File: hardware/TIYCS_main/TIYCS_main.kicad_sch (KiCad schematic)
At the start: 50 parts, among them J1 USB4105-GF-A, J2 12vPWM, J3 WS2812B, J4 UART, J5 ExtSensor, J6 Terminal, J7 Barrel_Jack_Switch, J8 pinHeaders, Q1 NCE4060K, Q2 NCE4060K, Q3 2N7002, Q4 NCE4060K, Q5 NCE4060K, SW1 SW_Push, SW2 SW_Push, U1 ESP32-WROOM-32U, U2 CH340N, U3 MCP1703A-3302_SOT23

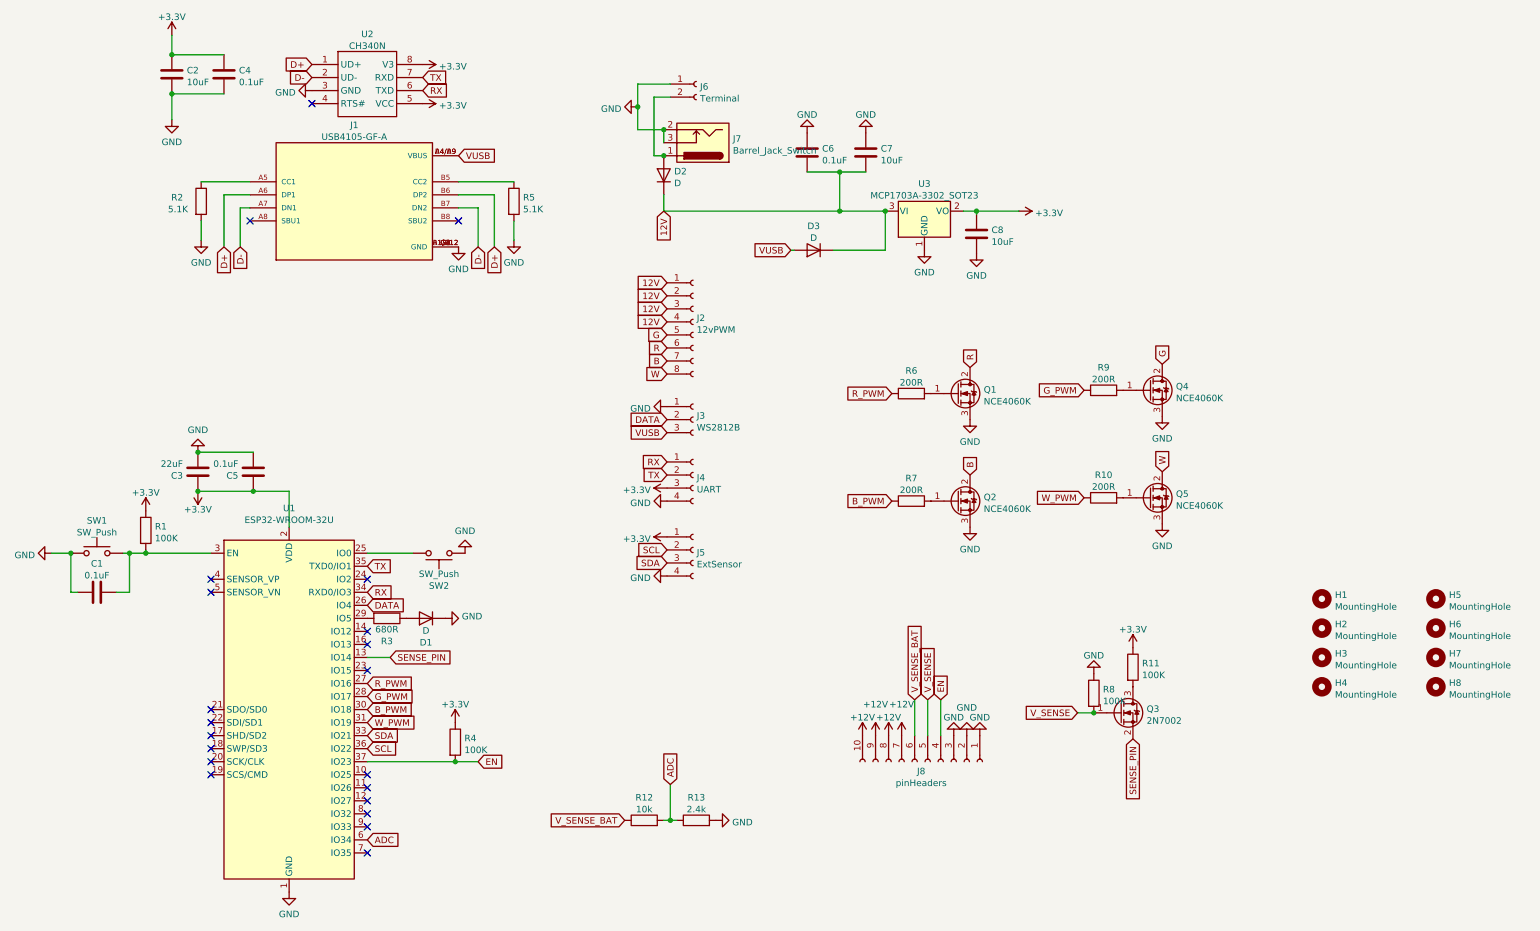
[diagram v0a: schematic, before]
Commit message: Start with new LDO, fuse
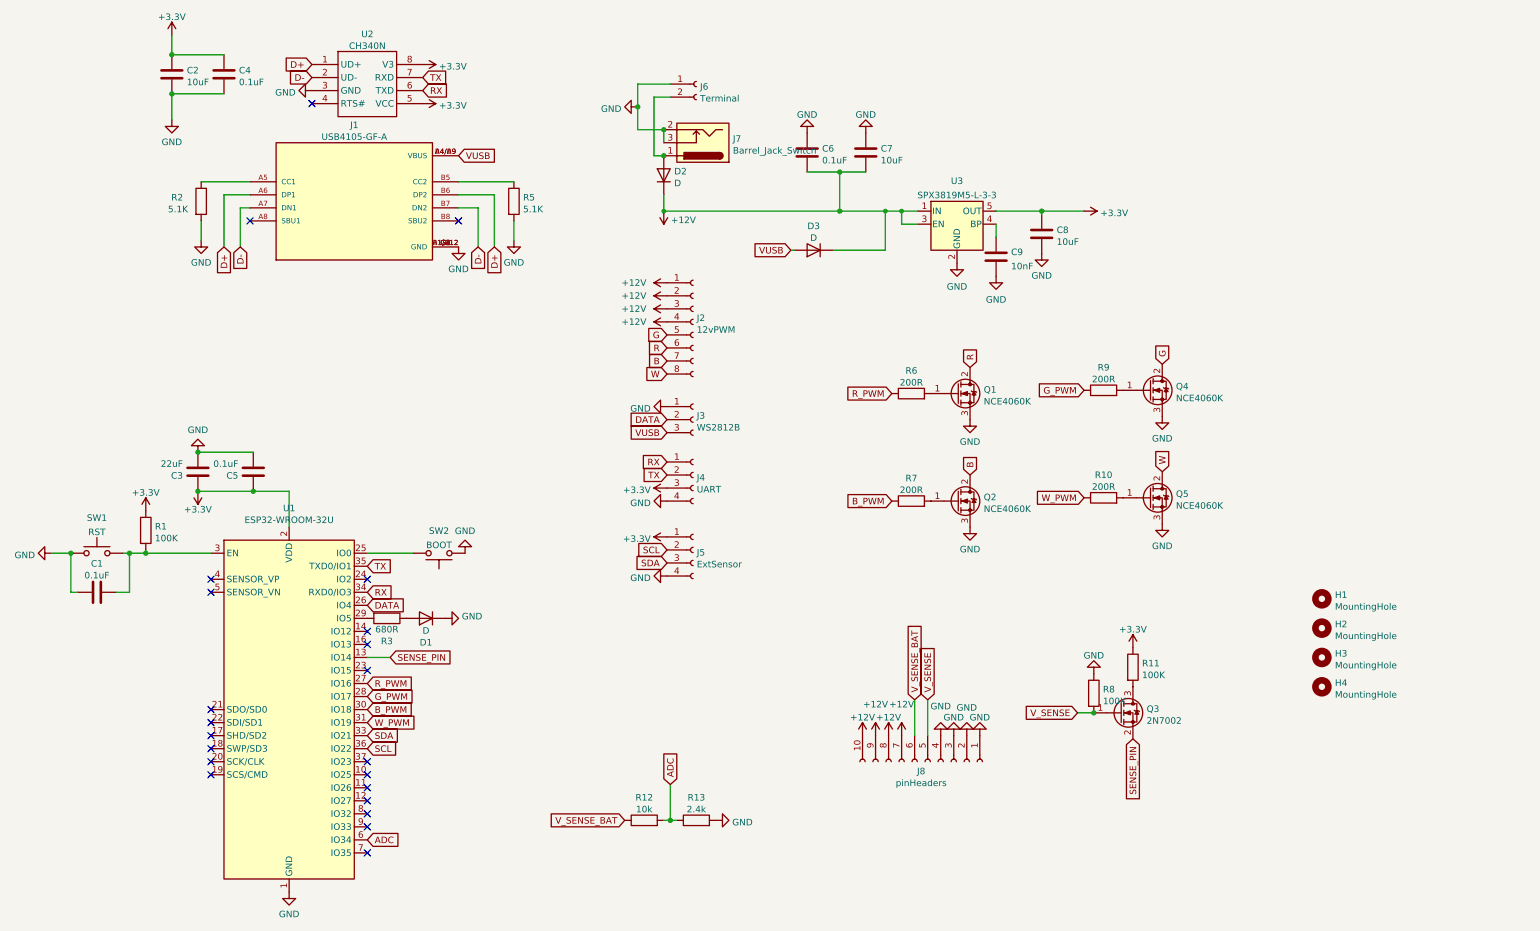
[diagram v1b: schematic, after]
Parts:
- removed H5, H6, H7, H8: MountingHole, MountingHole:MountingHole_3mm_Pad, symbol Mechanical:MountingHole
- removed R4: 100K, Resistor_SMD:R_0402_1005Metric, symbol Device:R
- removed U3: MCP1703A-3302_SOT23, Package_TO_SOT_SMD:SOT-23, symbol Regulator_Linear:MCP1703A-3302_SOT23
- added C9: 10nF, symbol Device:C
- added U3: SPX3819M5-L-3-3, Package_TO_SOT_SMD:SOT-23-5, symbol Regulator_Linear:SPX3819M5-L-3-3
- SW1: value SW_Push -> RST
- SW2: value SW_Push -> BOOT
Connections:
- net 12V is gone; now on net +12V: C6.2, C7.2, D2.1 (K), D3.1 (K), J2.1 (Pin_1), J2.2 (Pin_2), J2.3 (Pin_3), J2.4 (Pin_4)
- net +12V: now also U3.1 (IN), U3.3 (EN)
- net +3V3: now also U3.5 (OUT)
- net GND: now also J8.4 (Pin_4), C9.2, U3.2 (GND)
- net EN: no longer names the net of U1.37 (IO23)
- net EN: no longer J8.4 (Pin_4)
- new net: C9.1, U3.4 (BP)
- no-connect marks 21 -> 22
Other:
- moved on the sheet: C8

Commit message: First version of ledPanel: board outline + pins
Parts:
- C9: footprint (none) -> Capacitor_SMD:C_0402_1005Metric; JLCPCB (none) -> C15195
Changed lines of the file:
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@@
       (effects (font (size 1.27 1.27)) (justify left))
     )
-    (property "Footprint" "" (id 2) (at 208.6102 60.96 0)
+    (property "Footprint" "Capacitor_SMD:C_0402_1005Metric" (id 2) (at 208.6102 60.96 0)
       (effects (font (size 1.27 1.27)) hide)
     )
     (property "Datasheet" "~" (id 3) (at 207.645 57.15 0)
+      (effects (font (size 1.27 1.27)) hide)
+    )
+    (property "JLCPCB" " C15195 " (id 4) (at 207.645 57.15 0)
       (effects (font (size 1.27 1.27)) hide)
     )
@@
     )
     (path "/a6506404-fdc7-4490-bc6e-94643a9195be"
-      (reference "C9") (unit 1) (value "10nF") (footprint "")
+      (reference "C9") (unit 1) (value "10nF") (footprint "Capacitor_SMD:C_0402_1005Metric")
     )
     (path "/db090710-95ea-418e-b1d7-4e68f614b9ba"

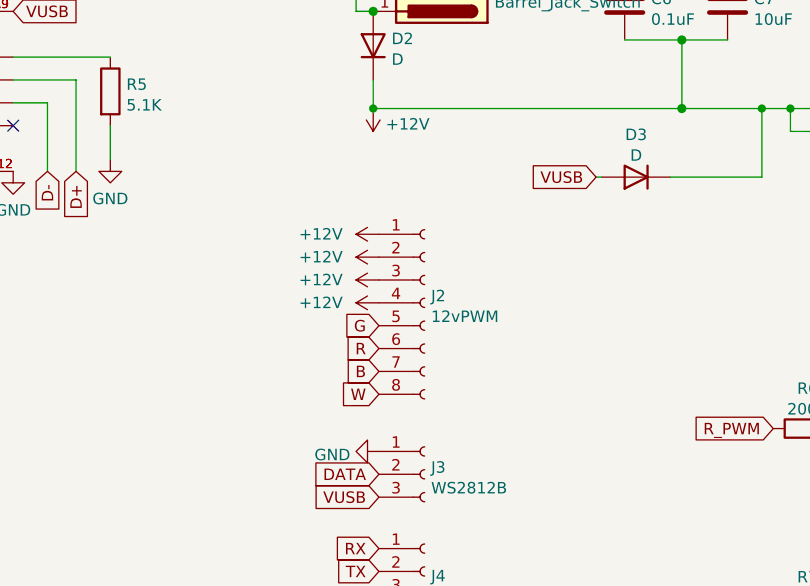
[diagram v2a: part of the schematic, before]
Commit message: Connector on motherboard aligned with ledPanel
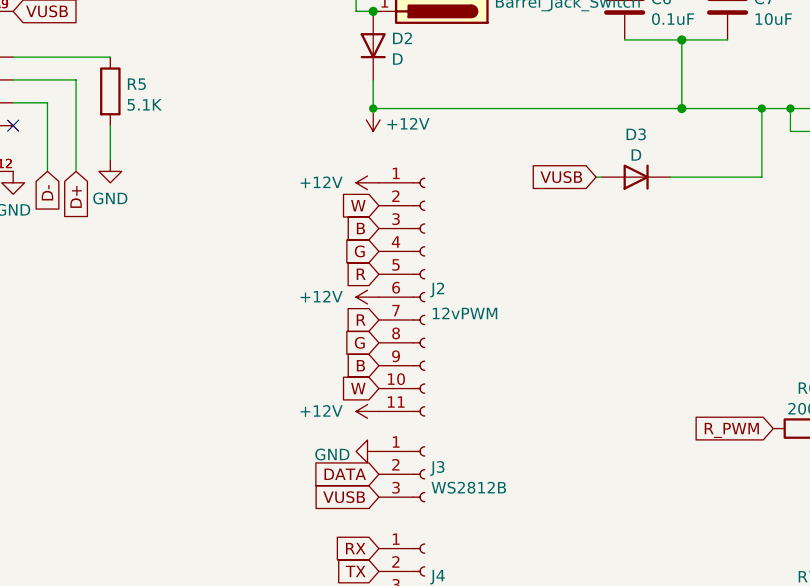
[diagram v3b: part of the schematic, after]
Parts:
- removed J2: 12vPWM, Connector_PinHeader_2.54mm:PinHeader_1x08_P2.54mm_Vertical, symbol Connector:Conn_01x08_Female
- added J2: 12vPWM, Connector_PinHeader_2.54mm:PinHeader_1x11_P2.54mm_Vertical, symbol Connector:Conn_01x11_Female
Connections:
- net +12V: now also J2.1 (Pin_1), J2.11 (Pin_11), J2.6 (Pin_6)
- net B: now also J2.3 (Pin_3), J2.9 (Pin_9)
- net G: now also J2.4 (Pin_4), J2.8 (Pin_8)
- net R: now also J2.5 (Pin_5), J2.7 (Pin_7)
- net W: now also J2.10 (Pin_10), J2.2 (Pin_2)

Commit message: Ordered hardware
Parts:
- added SW?: BTN, Switches:TACTILE_SWITCH_SMD_6.0X3.5MM, symbol Switch:SW_Push
- C2, C8: footprint Capacitor_SMD:C_0402_1005Metric -> Capacitor_SMD:C_0603_1608Metric
- C7: footprint Capacitor_SMD:C_0402_1005Metric -> Capacitor_SMD:C_0603_1608Metric; JLCPCB C15525 -> (none)
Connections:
- net GND: now also SW?.1
- net at U1.23 (IO15): now also SW?.2
- no-connect marks 22 -> 21
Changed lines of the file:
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@@
   (no_connect (at 85.09 120.015))
   (no_connect (at 85.09 132.715))
-  (no_connect (at 85.09 137.795))
   (no_connect (at 85.09 158.115))
   (no_connect (at 85.09 160.655))
@@
     (stroke (width 0) (type solid) (color 0 0 0 0))
   )
+  (wire (pts (xy 85.09 137.795) (xy 103.505 137.795))
+    (stroke (width 0) (type default) (color 0 0 0 0))
+  )
   (wire (pts (xy 207.645 50.8) (xy 207.645 53.34))
     (stroke (width 0) (type default) (color 0 0 0 0))
@@
       (effects (font (size 1.27 1.27)) (justify left))
     )
-    (property "Footprint" "Capacitor_SMD:C_0402_1005Metric" (id 2) (at 47.9552 25.4 0)
+    (property "Footprint" "Capacitor_SMD:C_0603_1608Metric" (id 2) (at 47.9552 25.4 0)
       (effects (font (size 1.27 1.27)) hide)
     )
@@
     )
     (property "Datasheet" "" (id 3) (at 202.565 109.855 0)
+      (effects (font (size 1.27 1.27)) hide)
+    )
+    (pin "1")
+  )
+  (symbol (lib_id "power:GND") (at 113.665 137.795 180) (unit 1)
+    (in_bom yes) (on_board yes) (fields_autoplaced)
+    (property "Reference" "#PWR?" (id 0) (at 113.665 131.445 0)
+      (effects (font (size 1.27 1.27)) hide)
+    )
+    (property "Value" "GND" (id 1) (at 113.665 133.4706 0))
+    (property "Footprint" "" (id 2) (at 113.665 137.795 0)
+      (effects (font (size 1.27 1.27)) hide)
+    )
+    (property "Datasheet" "" (id 3) (at 113.665 137.795 0)
       (effects (font (size 1.27 1.27)) hide)
     )
@@
     (pin "2")
   )
+  (symbol (lib_id "Switch:SW_Push") (at 108.585 137.795 180) (unit 1)
+    (in_bom yes) (on_board yes) (fields_autoplaced)
+    (property "Reference" "SW?" (id 0) (at 108.585 133.4475 0))
+    (property "Value" "BTN" (id 1) (at 108.585 136.2226 0))
+    (property "Footprint" "Switches:TACTILE_SWITCH_SMD_6.0X3.5MM" (id 2) (at 108.585 142.875 0)
+      (effects (font (size 1.27 1.27)) hide)
+    )
+    (property "Datasheet" "~" (id 3) (at 108.585 142.875 0)
+      (effects (font (size 1.27 1.27)) hide)
+    )
+    (pin "1")
+    (pin "2")
+  )
   (symbol (lib_id "Mechanical:MountingHole") (at 271.145 140.97 0) (unit 1)
     (in_bom yes) (on_board yes) (fields_autoplaced)
@@
       (effects (font (size 1.27 1.27)) (justify left))
     )
-    (property "Footprint" "Capacitor_SMD:C_0402_1005Metric" (id 2) (at 217.5002 56.515 0)
+    (property "Footprint" "Capacitor_SMD:C_0603_1608Metric" (id 2) (at 217.5002 56.515 0)
       (effects (font (size 1.27 1.27)) hide)
     )
@@
       (effects (font (size 1.27 1.27)) (justify left))
     )
-    (property "Footprint" "Capacitor_SMD:C_0402_1005Metric" (id 2) (at 183.2102 40.64 0)
+    (property "Footprint" "Capacitor_SMD:C_0603_1608Metric" (id 2) (at 183.2102 40.64 0)
       (effects (font (size 1.27 1.27)) hide)
     )
@@
       (effects (font (size 1.27 1.27)) hide)
     )
-    (property "JLCPCB" " C15525" (id 4) (at 182.245 36.83 0)
+    (property "JLCPCB" "" (id 4) (at 182.245 36.83 0)
       (effects (font (size 1.27 1.27)) hide)
     )
@@
       (reference "#PWR0147") (unit 1) (value "GND") (footprint "")
     )
+    (path "/a9cb1444-eba6-4ddf-88fb-081d86707002"
+      (reference "#PWR?") (unit 1) (value "GND") (footprint "")
+    )
     (path "/8c637d7d-c3ec-4153-9e1f-46e8fe712d7c"
       (reference "C1") (unit 1) (value "0.1uF") (footprint "Capacitor_SMD:C_0402_1005Metric")
     )
     (path "/6d23f2b3-8b15-4422-b7ea-fcbb1a61eb6b"
-      (reference "C2") (unit 1) (value "10uF") (footprint "Capacitor_SMD:C_0402_1005Metric")
+      (reference "C2") (unit 1) (value "10uF") (footprint "Capacitor_SMD:C_0603_1608Metric")
     )
     (path "/63c7647a-7f88-4811-aeb6-42a50ac287d8"
@@
     )
     (path "/e3e8dee4-7597-4ebc-89e5-4bbb58b34d69"
-      (reference "C7") (unit 1) (value "10uF") (footprint "Capacitor_SMD:C_0402_1005Metric")
+      (reference "C7") (unit 1) (value "10uF") (footprint "Capacitor_SMD:C_0603_1608Metric")
     )
     (path "/e130b0c6-1e03-41cc-9187-1a6306a02f14"
-      (reference "C8") (unit 1) (value "10uF") (footprint "Capacitor_SMD:C_0402_1005Metric")
+      (reference "C8") (unit 1) (value "10uF") (footprint "Capacitor_SMD:C_0603_1608Metric")
     )
     (path "/a6506404-fdc7-4490-bc6e-94643a9195be"
@@
       (reference "SW2") (unit 1) (value "BOOT") (footprint "Switches:TACTILE_SWITCH_SMD_6.0X3.5MM")
     )
+    (path "/d13e8b6d-8b82-4ae1-a8ab-4cc22756669a"
+      (reference "SW?") (unit 1) (value "BTN") (footprint "Switches:TACTILE_SWITCH_SMD_6.0X3.5MM")
+    )
     (path "/f3889d7e-5766-4016-abdb-86011b33eeb0"
